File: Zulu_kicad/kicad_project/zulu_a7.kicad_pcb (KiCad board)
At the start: 6 copper layers, 69.8 x 25.4 mm, 178 parts, among them J1 Pmod 2x6, Q1 12MHz 10ppm (FPGA + FT2232HL), U1 XC7A35T-1CPG236C, U10 93LC46BT-I/SN, U2 FT2232HL USB-UART/JTAG Bridge, U3 AS4C32M16SB-7TCN, U4 W25Q128JVSIQ, U5 SC189ZSKTRT, U6 SC189LSKTRT, U7 SC189ASKTRT, U8 BQ24232 LiPo charger + power 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, X1 Molex 105017-0001 Micro-USB-B, X2 ZULU-CONN, X3 DM3D-SF, X4 JST PH 2-pin, 1S LiPo

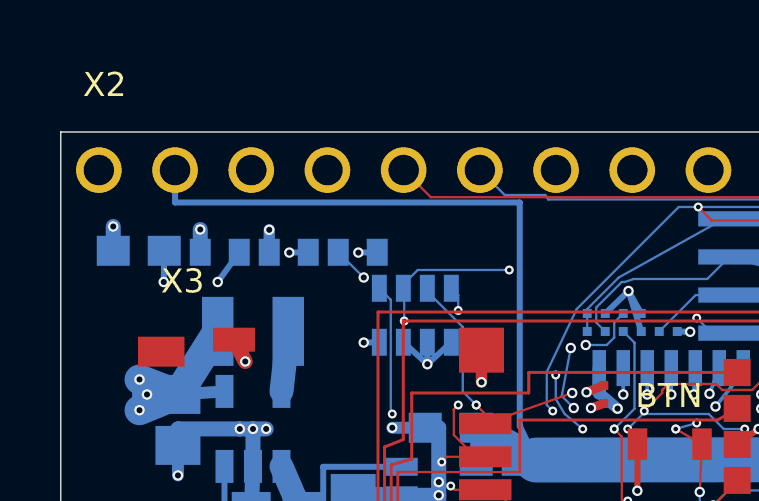
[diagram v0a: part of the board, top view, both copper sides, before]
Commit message: X2 power pins re-ordered on all copies; HDI copy gets the X1 land fix
X2 top row, at the user's request: 17 GND, 18 VCC3V3, 19 VCC1V8, 20 VCC1V0
(was 17 VCC3V3, 18 VCC1V8, 19 VCC1V0, 20 GND); pin 16 CHAN13 unchanged.

Altium (production and HDI_Optimized):
- zulu_a7_2.SchDoc via tools/x2_power_pins.py: four gate copies moved with
  their wires and labels, pins renumbered in all 41 copies, NOTE and frame
  reworded.
- PcbDoc via tools/X2PowerPins.pas: pads re-netted, VCC1V8 L3 stub moved to
  pin 19, VCC1V0 Bottom run extended to pin 20, planes repoured. ECO preview
  shows no net changes; only the X2 NOTE was imported.
- Post-save DRC 0/0 (production 14:28, HDI 14:34). Drill files
  byte-identical; copper differs only at X2's corner.
- Gerbers, drills, fab notes, zips and assembly notes/drawings regenerated;
  BOM and CPL unchanged.
- Production PcbDoc 517b553e, PCBWay zip FD44329E.
- HDI PcbDoc 71e75c10, zips 9C3E89E2 (JLC) / B679B6A3 (PCBWay).

KiCad: tools/apply_x2_pins_sch.py and apply_x2_pins_pcb.py. Netlist differs
in exactly the four pins, geometry identical to the Altium import, parity 0,
unconnected 0; reports regenerated.

HDI_Optimized also gets the X1 MS1/MS2 land and clearance fix (HdiX1Pads,
HdiX1Rules, HdiX1Lib): oblong 1.11x1.81 / 0.90x1.60 lands, CHAN12 re-routed
over the slots, PcbLib footprint updated. Fab notes now give the buried-via
land as 0.27 mm.

Master BOM regenerated: X2 note, and the 0.1 uF line gains C155-C159.

Co-Authored-By: Claude Opus 5.5 <noreply@anthropic.com>
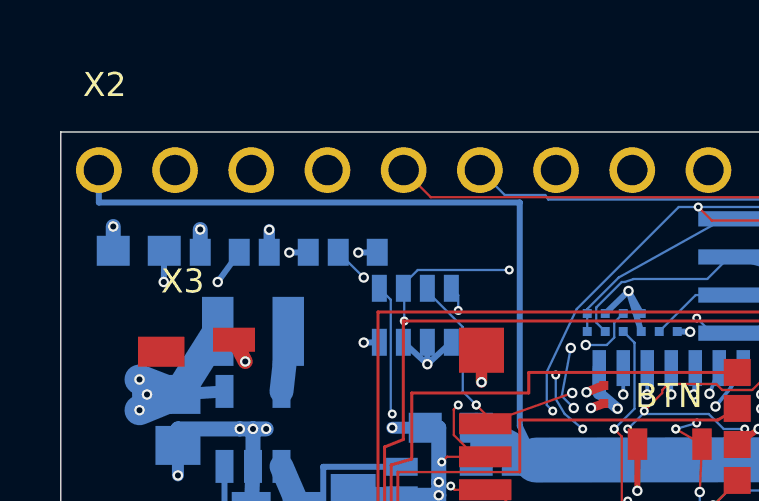
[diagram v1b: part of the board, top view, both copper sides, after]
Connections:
- X2 pad 17: VCC3V3 -> GND
- X2 pad 18: VCC1V8 -> VCC3V3
- X2 pad 19: VCC1V0 -> VCC1V8
- X2 pad 20: GND -> VCC1V0
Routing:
- net VCC1V0: track 125.0 -> 127.5 mm
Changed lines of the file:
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@@
 			)
 		)
-		(property "NOTE" "Pin field ZULU-DIP37: 40 pins of 1.016 mm on 2.54 mm pitch, two rows 22.86 mm (0.900 in) apart, numbered 1-40 straight through and skipping both landings. The rows are mirror images: top row pins 1-9 (x 59.69..39.37) = GND, CHAN-CLK, CHAN0..CHAN6, FOUR positions for the micro-USB X1 (36.83..29.21), pins 10-20 (26.67..1.27) = CHAN7..CHAN13, +3.3V, +1.8V, +1.0V, GND, in channel order since 2026-09-09; bottom row pins 21-29 (59.69..39.37), FOUR positions for the LiPo header X4 at the SAME four x values (36.83..29.21), pins 30-40 (26.67..1.27), so X4 sits on the top side directly opposite the edge-mounted USB receptacle. Each landing is 12.70 mm between the neighbouring pin centres, 11.176 mm clear: the JST B2B-PH-SM4-TB body is 7.95 mm, so 1.61 mm each side. Reworked 2026-09-09 from the old 44-position pattern: +5V-INPUT with D2/D3, GND5, GND3 and +3.3V2 removed, CHAN12/CHAN13 moved to pins 2/3, the bottom row closed up, the field renumbered and the landing moved. Three grounds (1, 20, 21); 3.3 V for the header is pin 17 alone; pin 22 VU sources the 4.4 V rail. THE PCB FOOTPRINT MUST BE REDRAWN with 40 pads named 1-40 in these positions -- the imported ZULU-DIP37 still names 44. Sullins PRPC strips fit the holes (0.64 mm square pins, Sullins recommends 1.02 mm). Digi-Key 2026-09-08: PRPC009SAAN-RC 1,201 at $0.18, PRPC011SAAN-RC 428 at $0.22, two of each per board (the 1x11 stock covers about 200 boards). Alternate: any 2.54 mm 1x40 breakaway strip (LCSC Boomele C2337, 81,690) cut to 9 + 11 twice."
+		(property "NOTE" "Pin field ZULU-DIP37: 40 pins of 1.016 mm on 2.54 mm pitch, two rows 22.86 mm (0.900 in) apart, numbered 1-40 straight through and skipping both landings. The rows are mirror images: top row pins 1-9 (x 59.69..39.37) = GND, CHAN-CLK, CHAN0..CHAN6, FOUR positions for the micro-USB X1 (36.83..29.21), pins 10-20 (26.67..1.27) = CHAN7..CHAN13, GND, +3.3V, +1.8V, +1.0V (channel order since 2026-09-09, power pins re-ordered 2026-10-07); bottom row pins 21-29 (59.69..39.37), FOUR positions for the LiPo header X4 at the SAME four x values (36.83..29.21), pins 30-40 (26.67..1.27), so X4 sits on the top side directly opposite the edge-mounted USB receptacle. Each landing is 12.70 mm between the neighbouring pin centres, 11.176 mm clear: the JST B2B-PH-SM4-TB body is 7.95 mm, so 1.61 mm each side. Reworked 2026-09-09 from the old 44-position pattern: +5V-INPUT with D2/D3, GND5, GND3 and +3.3V2 removed, CHAN12/CHAN13 moved to pins 2/3, the bottom row closed up, the field renumbered and the landing moved. Three grounds (1, 17, 21); 3.3 V for the header is pin 18 alone; pin 22 VU sources the 4.4 V rail. THE PCB FOOTPRINT MUST BE REDRAWN with 40 pads named 1-40 in these positions -- the imported ZULU-DIP37 still names 44. Sullins PRPC strips fit the holes (0.64 mm square pins, Sullins recommends 1.02 mm). Digi-Key 2026-09-08: PRPC009SAAN-RC 1,201 at $0.18, PRPC011SAAN-RC 428 at $0.22, two of each per board (the 1x11 stock covers about 200 boards). Alternate: any 2.54 mm 1x40 breakaway strip (LCSC Boomele C2337, 81,690) cut to 9 + 11 twice."
 			(at 0 0 0)
 			(layer "F.SilkS")
@@
 			(layers "*.Cu" "*.Mask")
 			(remove_unused_layers no)
-			(net "VCC3V3")
+			(net "GND")
 			(thermal_bridge_angle 90)
 			(padstack
@@
 			(layers "*.Cu" "*.Mask")
 			(remove_unused_layers no)
-			(net "VCC1V8")
+			(net "VCC3V3")
 			(thermal_bridge_angle 90)
 			(padstack
@@
 			(layers "*.Cu" "*.Mask")
 			(remove_unused_layers no)
-			(net "VCC1V0")
+			(net "VCC1V8")
 			(thermal_bridge_angle 90)
 			(padstack
@@
 			(layers "*.Cu" "*.Mask")
 			(remove_unused_layers no)
-			(net "GND")
+			(net "VCC1V0")
 			(thermal_bridge_angle 90)
 			(padstack
@@
 	)
 	(segment
-		(start 119.9261 94.6536)
-		(end 119.9261 93.5736)
+		(start 117.3861 94.6536)
+		(end 117.3861 93.5736)
 		(width 0.3)
 		(layer "In2.Cu")
@@
 	)
 	(segment
-		(start 117.3861 94.6536)
+		(start 114.8461 94.6536)
 		(end 128.8761 94.6536)
 		(width 0.2)
@@
 	)
 	(segment
-		(start 117.3861 94.6536)
-		(end 117.3861 93.5736)
+		(start 114.8461 94.6536)
+		(end 114.8461 93.5736)
 		(width 0.2)
 		(layer "B.Cu")

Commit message: PCBWay assembly release; X2 pin labels on the top silkscreen (all copies)
Assembly (production): tools/generate_jlcpcb_assembly.py gains
--assembler {pcbway,jlcpcb,neutral}; pcbway is the default, jlcpcb still
reproduces the old files byte for byte.
- BOM renamed to Zulu_A7_PCBWay_BOM.csv: PCBWay template columns, MPN
  identities (no LCSC, no "consign"), X2 split into PRPC009 x2 + PRPC011
  x2, JP3/JP4 DNS rows, per-line instructions.
- CPL renamed to Zulu_A7_PCBWay_CPL.csv: SMT parts only.
- Assembly notes rewritten for a PCBWay turnkey order: form settings,
  panel, U1 via plugging, reflow order (X1 one reflow), X2 orientation,
  X1 stakes, LED polarity, sourcing.
- Drawings mark LED cathodes.
- Fab notes: X1 slots are the front shell stakes (not "rear"); U1 via
  wording fixed and plugging requested.

X2 labels: pin number + short name for 33 pins, top silkscreen, 0.8 mm
stroke text (PCBWay minimum); pins 1 and 4-9 have no room.
- Moved: U2 designator; X3 designator (production); ZULU A7 title (HDI).
- DRC 0/0 incl. silk rules; only GTO changed.
- Production PcbDoc bd7cbfd7, PCBWay zip 7EEACEFC.
- HDI PcbDoc a3436176, zips 5F68EC18 / D28EE93C.
- KiCad: tools/apply_x2_labels.py, parity 0.

Verified by an independent three-checker workflow; its minor findings
were fixed.

Co-Authored-By: Claude Opus 5.5 <noreply@anthropic.com>
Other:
- board text added: "10"
- board text added: "11"
- board text added: "12"
- board text added: "13"
- board text added: "14"
- board text added: "15"
- board text added: "16"
- board text added: "17"
- board text added: "18"
- board text added: "19"
- board text added: "1V0"
- board text added: "1V8"
- board text added: "2 CLK"
- board text added: "20"
- board text added: "21 GND"
- board text added: "22"
- board text added: "23"
- board text added: "24"
- board text added: "25"
- board text added: "26"
- board text added: "27"
- board text added: "28"
- board text added: "29"
- board text added: "3"
- board text added: "30 C20"
- board text added: "31"
- board text added: "32"
- board text added: "33"
- board text added: "34"
- board text added: "35"
- board text added: "36"
- board text added: "37"
- board text added: "38"
- board text added: "39"
- board text added: "3V3"
- board text added: "40"
- board text added: "AI0"
- board text added: "AI1"
- board text added: "C0"
- board text added: "C10"
- board text added: "C11"
- board text added: "C12"
- board text added: "C13"
- board text added: "C14"
- board text added: "C15"
- board text added: "C16"
- board text added: "C17"
- board text added: "C18"
- board text added: "C19"
- board text added: "C21"
- board text added: "C22"
- board text added: "C23"
- board text added: "C24"
- board text added: "C25"
- board text added: "C26"
- board text added: "C27"
- board text added: "C28"
- board text added: "C7"
- board text added: "C8"
- board text added: "C9"
- board text added: "GND"
- board text added: "RST"
- board text added: "VU"

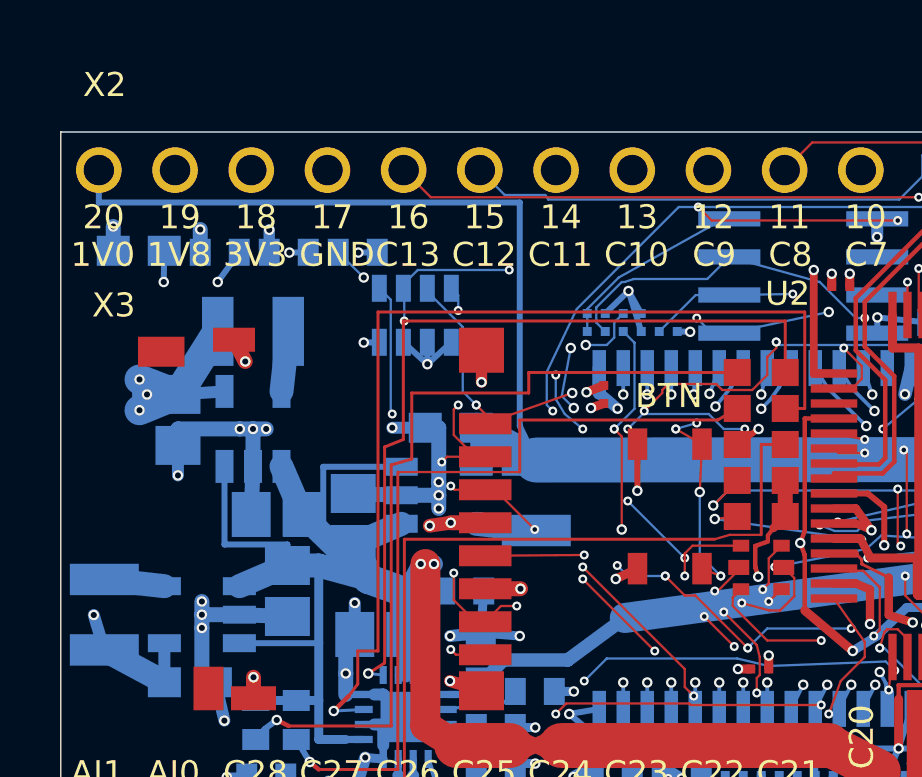
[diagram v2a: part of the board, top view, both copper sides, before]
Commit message: Move BTN 0.5 mm left and hide the X2 designator (all copies)
BTN (PTS810) moves from x 20.3 to 19.8 mm, away from the RGB LEDs: pad gap
to LD5 0.40 -> 0.90 mm. Three via stacks left its new pad field, pad 1's
VCC3V3 through via became a Top>L5 microvia stack, 14 tracks were re-drawn
and 3 added. Three filled Top-L2 microvias now overlap BTN pads 1/3/4, the
board's only via-in-pad; the fab notes ask for VIPPO.

- Production PcbDoc 89a421b9, HDI f97d0f4d: Altium DRC 0/0 after save;
  new laser vias marked microvia (stage13_mark_microvias.py).
- Gerbers/NC drill regenerated; changes confined to the BTN area plus the
  removed X2 designator. Fab notes, packager counts and all three zips
  updated; assembly CPL changes only BTN's row.
- KiCad: apply_btn_move.py, geom_diff IDENTICAL to a fresh import,
  parity 0, unconnected 0.
- docs/btn_move.md, HDI_OPTIMIZATION_NOTES.md, CONVERSION.md.

Co-Authored-By: Claude Opus 5.5 <noreply@anthropic.com>
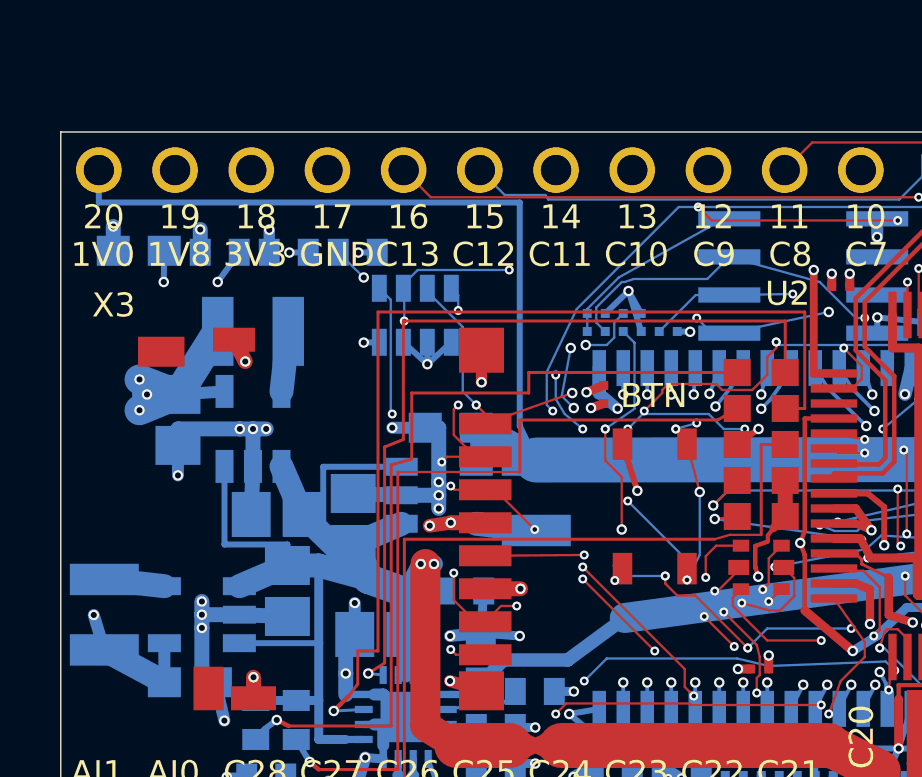
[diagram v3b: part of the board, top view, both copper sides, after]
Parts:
- moved BTN 0.50 mm to (133.4, 104.8)
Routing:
- net LED0_B: track 50.6 -> 49.6 mm
- net N$BTN: track 26.3 -> 25.7 mm
- net FT-RESETN: track 22.0 -> 22.5 mm
- net VCC3V3: track 165.4 -> 165.1 mm, vias 85 -> 88
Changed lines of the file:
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@@
 	(footprint "zulu_a7:PTS810"
 		(layer "F.Cu")
-		(at 133.87613 104.78357 90)
+		(at 133.37613 104.78357 90)
 		(property "Reference" "BTN"
 			(at 3.682216 -0.02829 0)
@@
 			(unlocked yes)
 			(layer "F.SilkS")
+			(hide yes)
 			(effects
 				(font
@@
 	)
 	(segment
+		(start 135.0761 107.1536)
+		(end 135.0761 106.4436)
+		(width 0.0762)
+		(layer "F.Cu")
+		(net "LED0_B")
+	)
+	(segment
 		(start 149.4761 110.2036)
 		(end 150.0261 109.6536)
@@
 	)
 	(segment
-		(start 134.636 106.0937)
-		(end 136.2512 106.0937)
+		(start 135.0761 106.4436)
+		(end 135.4261 106.0936)
 		(width 0.0762)
 		(layer "F.Cu")
@@
 	)
 	(segment
-		(start 134.3761 106.3536)
-		(end 134.636 106.0937)
-		(width 0.0762)
-		(layer "F.Cu")
-		(net "LED0_B")
-	)
-	(segment
 		(start 150.0261 109.6536)
 		(end 150.4761 109.6536)
@@
 	)
 	(segment
-		(start 134.3761 107.1036)
-		(end 134.3761 106.3536)
+		(start 135.4261 106.0936)
+		(end 136.2512 106.0937)
 		(width 0.0762)
 		(layer "F.Cu")
@@
 	)
 	(via blind
-		(at 134.3761 107.1036)
+		(at 135.0761 107.1536)
 		(size 0.3)
 		(drill 0.15)
@@
 	)
 	(via buried
-		(at 134.3761 107.1036)
+		(at 149.4761 110.2036)
 		(size 0.3)
 		(drill 0.15)
@@
 	)
 	(via buried
-		(at 149.4761 110.2036)
+		(at 135.0761 107.1536)
 		(size 0.3)
 		(drill 0.15)
@@
 	)
 	(segment
-		(start 134.3761 107.1036)
-		(end 135.0261 107.7536)
-		(width 0.0762)
-		(layer "In2.Cu")
-		(net "LED0_B")
-	)
-	(segment
 		(start 154.2761 106.6036)
 		(end 155.5761 106.6036)
@@
 	)
 	(segment
+		(start 135.0261 107.7536)
+		(end 135.0761 107.1536)
+		(width 0.0762)
+		(layer "In2.Cu")
+		(net "LED0_B")
+	)
+	(segment
 		(start 149.1761 110.2036)
 		(end 149.4761 110.2036)
@@
 	)
 	(segment
+		(start 132.0461 107.2536)
+		(end 132.3011 106.8586)
+		(width 0.3)
+		(layer "F.Cu")
+		(net "VCC3V3")
+	)
+	(segment
 		(start 136.126 102.7186)
 		(end 136.8361 102.2036)
@@
 	)
 	(segment
-		(start 132.7961 104.2636)
-		(end 132.8012 102.7086)
-		(width 0.2)
-		(layer "F.Cu")
-		(net "VCC3V3")
-	)
-	(segment
 		(start 160.2262 110.8036)
 		(end 160.2262 110.0536)
@@
 	)
 	(segment
-		(start 132.0761 107.2036)
-		(end 132.8011 106.8586)
-		(width 0.3)
-		(layer "F.Cu")
-		(net "VCC3V3")
-	)
-	(segment
 		(start 161.4761 106.3036)
 		(end 161.4761 105.8037)
@@
 	)
 	(segment
+		(start 132.3011 102.7086)
+		(end 132.7961 104.2636)
+		(width 0.2)
+		(layer "F.Cu")
+		(net "VCC3V3")
+	)
+	(segment
 		(start 145.3011 99.4236)
 		(end 148.3011 99.4236)
@@
 	)
 	(via
-		(at 132.0761 107.2036)
-		(size 0.35)
-		(drill 0.2)
-		(layers "F.Cu" "B.Cu")
-		(tenting
-			(front yes)
-			(back yes)
-		)
-		(net "VCC3V3")
-	)
-	(via
 		(at 154.4261 102.1036)
 		(size 0.35)
@@
 		(net "VCC3V3")
 	)
+	(via blind
+		(at 132.0461 107.2536)
+		(size 0.3)
+		(drill 0.15)
+		(layers "F.Cu" "In1.Cu")
+		(tenting
+			(front yes)
+			(back yes)
+		)
+		(net "VCC3V3")
+	)
 	(via
 		(at 160.1261 97.4536)
@@
 		(net "VCC3V3")
 	)
+	(via buried
+		(at 132.0461 107.2536)
+		(size 0.3)
+		(drill 0.15)
+		(layers "In1.Cu" "In2.Cu")
+		(tenting
+			(front yes)
+			(back yes)
+		)
+		(net "VCC3V3")
+	)
+	(via buried
+		(at 132.0461 107.2536)
+		(size 0.27)
+		(drill 0.15)
+		(layers "In2.Cu" "In3.Cu")
+		(tenting
+			(front yes)
+			(back yes)
+		)
+		(net "VCC3V3")
+	)
+	(via buried
+		(at 132.0461 107.2536)
+		(size 0.3)
+		(drill 0.15)
+		(layers "In3.Cu" "In4.Cu")
+		(tenting
+			(front yes)
+			(back yes)
+		)
+		(net "VCC3V3")
+	)
 	(segment
 		(start 152.5761 95.7036)
@@
 	)
 	(segment
-		(start 133.7261 107.1036)
-		(end 134.3761 107.7536)
+		(start 133.7261 107.3536)
+		(end 134.1261 107.7536)
 		(width 0.0762)
 		(layer "F.Cu")
@@
 	)
 	(segment
+		(start 131.7261 103.2536)
+		(end 131.7261 102.2036)
+		(width 0.0762)
+		(layer "F.Cu")
+		(net "FT-RESETN")
+	)
+	(segment
 		(start 139.4261 106.9286)
 		(end 140.3261 106.9286)
@@
 	)
 	(segment
+		(start 131.7261 103.2536)
+		(end 132.2761 103.8036)
+		(width 0.0762)
+		(layer "F.Cu")
+		(net "FT-RESETN")
+	)
+	(segment
+		(start 133.7261 107.3536)
+		(end 133.7261 107.1036)
+		(width 0.0762)
+		(layer "F.Cu")
+		(net "FT-RESETN")
+	)
+	(segment
 		(start 132.2761 105.5536)
-		(end 132.2761 102.4536)
+		(end 132.2761 103.8036)
 		(width 0.0762)
 		(layer "F.Cu")
@@
 	)
 	(segment
-		(start 132.0261 102.2036)
-		(end 132.2761 102.4536)
+		(start 134.1261 107.7536)
+		(end 134.3761 107.7536)
 		(width 0.0762)
 		(layer "F.Cu")
@@
 	)
 	(via blind
-		(at 132.0261 102.2036)
+		(at 131.7261 102.2036)
 		(size 0.3)
 		(drill 0.15)
@@
 	)
 	(segment
-		(start 132.0261 102.2036)
-		(end 132.7011 101.5286)
-		(width 0.0762)
-		(layer "B.Cu")
-		(net "FT-RESETN")
-	)
-	(segment
 		(start 132.326 98.9536)
 		(end 132.7011 99.3287)
@@
 		(net "FT-RESETN")
 	)
+	(segment
+		(start 131.7261 102.2036)
+		(end 132.7011 101.5286)
+		(width 0.0762)
+		(layer "B.Cu")
+		(net "FT-RESETN")
+	)
 	(via buried
-		(at 132.0261 102.2036)
+		(at 140.6761 109.1036)
 		(size 0.3)
 		(drill 0.15)
@@
 	)
 	(via buried
-		(at 140.6761 109.1036)
+		(at 131.7261 102.2036)
 		(size 0.3)
 		(drill 0.15)
@@
 	)
 	(via buried
-		(at 132.0261 102.2036)
+		(at 131.7261 102.2036)
 		(size 0.27)
 		(drill 0.15)
@@
 	)
 	(via buried
-		(at 132.0261 102.2036)
+		(at 133.7261 107.1036)
 		(size 0.3)
 		(drill 0.15)
@@
 	)
 	(via buried
-		(at 133.7261 107.1036)
+		(at 131.7261 102.2036)
 		(size 0.3)
 		(drill 0.15)
@@
 	)
 	(via blind
-		(at 132.0261 102.2036)
+		(at 136.4761 109.5036)
 		(size 0.3)
 		(drill 0.15)
@@
 	)
 	(via blind
-		(at 136.4761 109.5036)
+		(at 131.7261 102.2036)
 		(size 0.3)
 		(drill 0.15)
@@
 	)
 	(segment
-		(start 134.8761 104.3036)
-		(end 134.9511 102.7086)
+		(start 134.4511 107.2336)
+		(end 134.4511 106.8586)
 		(width 0.0762)
 		(layer "F.Cu")
@@
 	)
 	(segment
-		(start 134.9511 106.8585)
-		(end 135.5761 107.1036)
+		(start 134.4511 102.7086)
+		(end 134.8761 104.3036)
 		(width 0.0762)
 		(layer "F.Cu")
@@
 	(segment
 		(start 134.0761 102.2036)
-		(end 134.9511 102.7086)
+		(end 134.4511 102.7086)
 		(width 0.0762)
 		(layer "F.Cu")
@@
 	)
 	(via blind
-		(at 134.0761 102.2036)
+		(at 134.4511 107.2336)
 		(size 0.3)
 		(drill 0.15)
@@
 	)
 	(via blind
-		(at 135.5761 107.1036)
+		(at 134.0761 102.2036)
 		(size 0.3)
 		(drill 0.15)
@@
 	)
 	(segment
-		(start 134.0761 102.2036)
-		(end 134.7761 102.0036)
+		(start 134.4511 107.2336)
+		(end 134.8761 106.4036)
 		(width 0.0762)
 		(layer "B.Cu")
@@
 	)
 	(segment
-		(start 134.8761 106.4036)
-		(end 135.5761 107.1036)
+		(start 134.0761 102.2036)
+		(end 134.7761 102.0036)
 		(width 0.0762)
 		(layer "B.Cu")
@@
 	)
 	(via buried
-		(at 135.5761 107.1036)
+		(at 134.4511 107.2336)
 		(size 0.3)
 		(drill 0.15)
@@
 	)
 	(via buried
-		(at 135.5761 107.1036)
+		(at 140.5761 99.1036)
 		(size 0.27)
 		(drill 0.15)
@@
 	)
 	(via buried
-		(at 140.5761 99.1036)
+		(at 146.0761 96.4036)
 		(size 0.27)
 		(drill 0.15)
@@
 	)
 	(via buried
-		(at 146.0761 96.4036)
+		(at 134.0761 102.2036)
 		(size 0.27)
 		(drill 0.15)
@@
 	)
 	(via buried
-		(at 134.0761 102.2036)
+		(at 134.4511 107.2336)
 		(size 0.27)
 		(drill 0.15)
@@
 	)
 	(via buried
-		(at 134.0761 102.2036)
+		(at 134.4511 107.2336)
 		(size 0.3)
 		(drill 0.15)
@@
 	)
 	(via buried
-		(at 134.7761 102.0036)
+		(at 134.0761 102.2036)
 		(size 0.3)
 		(drill 0.15)
@@
 	)
 	(via buried
-		(at 135.5761 107.1036)
+		(at 134.7761 102.0036)
 		(size 0.3)
 		(drill 0.15)
@@
 	)
 	(via blind
-		(at 135.5761 107.1036)
+		(at 134.4511 107.2336)
 		(size 0.3)
 		(drill 0.15)
